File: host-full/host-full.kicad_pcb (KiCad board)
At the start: 4 copper layers, 117 x 129.5 mm, 201 parts, among them J1 CONN_INTEGRALSTICK_MCU_HOST, J10 PMOD_HOST, J11 PMOD_HOST, J12 PMOD_HOST, J13 PMOD_HOST, J14 PMOD_HOST, J15 XILINX_JTAG, J16 SMA, J17 SMA, J18 SMA, J19 SMA, J2 CONN_INTEGRALSTICK_FPGA_HOST, J20 SMA, J21 SMA, J22 TESTPAD, J23 PMOD_HOST, J24 TESTPAD, J25 TESTPAD, J26 TESTPAD, J27 TESTPAD, J28 TESTPAD, J29 TESTCLIP, J3 0826-1G1T-23-F, J30 TESTCLIP, J31 TESTCLIP, J4 0826-1G1T-23-F, J5 0826-1G1T-23-F, J6 0826-1G1T-23-F, J7 PMOD_HOST, J8 PMOD_HOST, J9 PMOD_HOST, K1 CONN_3_PWROUT, SW1 SW_SPST, SW2 SW_SPST, SW3 SW_SPST, U1 KSZ9031RNX, U2 KSZ9031RNX, U3 ECS-1612MV-250-CN-TR, U4 ECS-1612MV-250-CN-TR, U5 KSZ9031RNX, U6 ECS-1612MV-250-CN-TR, U7 SC185EUL

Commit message: Continued host-full layout. Almost all PHY RGMII routing done
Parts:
- added G***: LOGO, w_logo:Logo_silk_ROHS_5x2.8mm, F.Cu at (128.8, 89.8)
- added G***: LOGO, w_logo:Logo_silk_WEEE_3.4x5mm, F.Cu at (58.5, 41.8)
- added G***: LOGO, w_logo:Logo_silk_OSHW_6x6mm, F.Cu at (81.8, 40.8)
- added REF**: SERIALNUM_MOLEX_0916580020, azonenberg_pcb:SERIALNUM_MOLEX_0916580020, F.Cu at (34.5, 46.2)
- C10, C12, C14, C15, C16, C18, C19, C20, C22, C23, C24, C26, C28, C29, C30, C31, C32, C33, C34, C4, C59, C6, C60, C61, C62, C63, C64, C65, C66, C72, C73, C8, L4, R10, R20, R39, R40, R41, R42, R46, R47, R49, R50, R51: moved to B.Cu
- moved C40 57.0 mm to (50.8, 177.3)
- moved C42 57.0 mm to (48.1, 170.3)
- moved C45 57.0 mm to (32.2, 181.9)
- moved C50 57.0 mm to (32.4, 184.9)
- moved C51 57.0 mm to (40.5, 186.5)
- moved C52 57.0 mm to (38.0, 185.5)
- moved C54 57.0 mm to (31.5, 187.8)
- moved C69 57.0 mm to (39.2, 168.9)
- moved C83 57.0 mm to (41.8, 171.4)
- moved C84 57.0 mm to (46.2, 186.3)
- moved R32 57.0 mm to (29.8, 177.9)
- moved R36 57.0 mm to (32.6, 166.9)
- moved C39 57.0 mm to (35.2, 183.0)
- moved C47 57.0 mm to (45.5, 171.1)
- moved C48 57.0 mm to (44.9, 168.6)
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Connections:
- C10 pad 1: /1V8 -> /3V3
- C18 pad 1: /1V8 -> /3V3
- C2 pad 1: /1V8 -> /3V3
- C35 pad 1: /1V8 -> /3V3
- C38 pad 1: /3V3 -> /1V8
- C42 pad 1: /3V3 -> /1V8
- C46 pad 1: /3V3 -> /1V8
- C54 pad 1: /3V3 -> /1V8
- J1 pad 16: /Ethernet/ETH0_3_P -> /Ethernet/ETH0_3_N
- J1 pad 18: /Ethernet/ETH0_3_N -> /Ethernet/ETH0_3_P
- J1 pad 4: /Ethernet/ETH0_1_P -> /Ethernet/ETH0_1_N
- J1 pad 6: /Ethernet/ETH0_1_N -> /Ethernet/ETH0_1_P
- J18 pad 1: /LVDS_DQ0_P -> /LVDS_DQ1_N
- J19 pad 1: /LVDS_DQ0_N -> /LVDS_DQ1_P
- J2 pad 10: (no net) -> /LVDS_DQ8_N
- J2 pad 101: /Ethernet/ETH3_TXD2 -> /Ethernet/ETH1_TX_CLK
- J2 pad 102: /Ethernet/ETH3_TXD3 -> /Ethernet/ETH2_RXD3
- J2 pad 103: /Ethernet/ETH3_TX_CLK -> /Ethernet/ETH1_TXD3
- J2 pad 104: /Ethernet/ETH3_TX_EN -> /Ethernet/ETH2_TX_EN
- J2 pad 108: /Ethernet/ETH3_RXD3 -> /Ethernet/ETH2_TX_CLK
- J2 pad 110: /Ethernet/ETH3_RXD2 -> /Ethernet/ETH2_TXD3
- J2 pad 113: /Ethernet/ETH3_RXD1 -> /Ethernet/ETH1_TXD2
- J2 pad 114: /Ethernet/ETH3_RXD0 -> /Ethernet/ETH2_TXD2
- J2 pad 115: /Ethernet/ETH3_RX_DV -> /Ethernet/ETH1_TXD1
- J2 pad 116: /Ethernet/ETH3_MDC -> /Ethernet/ETH2_TXD1
- J2 pad 119: /Ethernet/ETH3_MDIO -> /Ethernet/ETH1_TXD0
- J2 pad 12: (no net) -> /LVDS_DQ8_P
- J2 pad 120: /Ethernet/ETH3_RST_N -> /Ethernet/ETH2_TXD0
- J2 pad 16: (no net) -> /LVDS_DQ6_N
- J2 pad 18: (no net) -> /LVDS_DQ6_P
- J2 pad 21: /LVDS_DQ5_N -> (no net)
- J2 pad 23: /LVDS_DQ5_P -> (no net)
- J2 pad 27: /LVDS_DQ3_N -> (no net)
- J2 pad 29: /LVDS_DQ3_P -> (no net)
- J2 pad 41: /Ethernet/ETH1_RX_CLK -> /Ethernet/ETH3_RX_CLK
- J2 pad 42: /Ethernet/ETH1_TXD0 -> /Ethernet/ETH3_MDIO
- J2 pad 43: /Ethernet/ETH1_LED1_N_1V8 -> /Ethernet/ETH3_MDC
- J2 pad 44: /Ethernet/ETH1_TXD1 -> /Ethernet/ETH3_RST_N
- J2 pad 47: /Ethernet/ETH1_TXD2 -> /Ethernet/ETH3_RX_DV
- J2 pad 48: /Ethernet/ETH1_TXD3 -> (no net)
- J2 pad 49: /Ethernet/ETH1_TX_CLK -> /Ethernet/ETH3_RXD0
- J2 pad 50: /Ethernet/ETH1_TX_EN -> /Ethernet/ETH3_LED2_N_1V8
- J2 pad 53: /Ethernet/ETH1_RST_N -> /Ethernet/ETH3_RXD1
- J2 pad 54: (no net) -> /Ethernet/ETH3_LED1_N_1V8
- J2 pad 55: (no net) -> /Ethernet/ETH3_RXD2
- J2 pad 56: /Ethernet/ETH1_MDC -> (no net)
- J2 pad 59: /Ethernet/ETH1_MDIO -> /Ethernet/ETH3_RXD3
- J2 pad 60: /Ethernet/ETH1_RXD3 -> (no net)
- J2 pad 61: /Ethernet/ETH1_RXD2 -> /Ethernet/ETH3_TXD2
- J2 pad 62: /Ethernet/ETH1_RXD1 -> /Ethernet/ETH3_TX_EN
- J2 pad 65: /Ethernet/ETH1_RXD0 -> /Ethernet/ETH3_TXD1
- J2 pad 66: /Ethernet/ETH1_RX_DV -> /Ethernet/ETH3_TX_CLK
- J2 pad 67: /Ethernet/ETH1_LED2_N_1V8 -> /Ethernet/ETH3_TXD0
- J2 pad 68: (no net) -> /Ethernet/ETH3_TXD3
- J2 pad 71: /Ethernet/ETH2_RX_CLK -> /Ethernet/ETH1_RX_CLK
- J2 pad 72: /Ethernet/ETH3_RX_CLK -> /Ethernet/ETH2_RX_CLK
- J2 pad 73: /Ethernet/ETH2_TXD0 -> /Ethernet/ETH1_RST_N
- J2 pad 74: /Ethernet/ETH2_TXD1 -> /Ethernet/ETH3_LED2_N
- J2 pad 77: /Ethernet/ETH2_TXD2 -> /Ethernet/ETH1_MDIO
- J2 pad 78: /Ethernet/ETH2_TXD3 -> /Ethernet/ETH3_LED1_N
- J2 pad 79: /Ethernet/ETH2_TX_CLK -> /Ethernet/ETH1_MDC
- J2 pad 80: /Ethernet/ETH2_TX_EN -> /Ethernet/ETH2_RST_N
- J2 pad 83: /Ethernet/ETH2_RXD3 -> /Ethernet/ETH1_RX_DV
- J2 pad 84: /Ethernet/ETH2_RXD2 -> /Ethernet/ETH2_MDIO
- J2 pad 85: /Ethernet/ETH2_RXD1 -> /Ethernet/ETH1_RXD0
- J2 pad 86: /Ethernet/ETH2_RXD0 -> /Ethernet/ETH2_MDC
- J2 pad 89: /Ethernet/ETH2_RX_DV -> /Ethernet/ETH1_RXD1
- J2 pad 90: /Ethernet/ETH2_MDC -> /Ethernet/ETH2_RX_DV
- J2 pad 91: /Ethernet/ETH2_MDIO -> /Ethernet/ETH1_RXD2
- J2 pad 92: /Ethernet/ETH2_RST_N -> /Ethernet/ETH2_RXD0
- J2 pad 95: /Ethernet/ETH1_LED1_N -> /Ethernet/ETH1_RXD3
- J2 pad 96: /Ethernet/ETH1_LED2_N -> /Ethernet/ETH2_RXD1
- J2 pad 97: /Ethernet/ETH3_TXD0 -> /Ethernet/ETH1_TX_EN
- J2 pad 98: /Ethernet/ETH3_TXD1 -> /Ethernet/ETH2_RXD2
- J20 pad 1: /LVDS_DQ1_P -> /LVDS_DQ0_N
- J21 pad 1: /LVDS_DQ1_N -> /LVDS_DQ0_P
- J23 pad 1: /LVDS_DQ2_P -> /LVDS_DQ8_N
- J23 pad 10: /LVDS_DQ5_N -> /LVDS_DQ2_P
- J23 pad 2: /LVDS_DQ2_N -> /LVDS_DQ8_P
- J23 pad 3: /LVDS_DQ3_P -> /LVDS_DQ4_N
- J23 pad 4: /LVDS_DQ3_N -> /LVDS_DQ4_P
- J23 pad 7: /LVDS_DQ4_P -> /LVDS_DQ6_N
- J23 pad 8: /LVDS_DQ4_N -> /LVDS_DQ6_P
- J23 pad 9: /LVDS_DQ5_P -> /LVDS_DQ2_N
- R1 pad 2: /Ethernet/ETH1_LED2_N_1V8 -> /Ethernet/ETH1_LED2_N
- R17 pad 1: /1V8 -> /3V3
- R19 pad 2: /Ethernet/ETH1_LED1_N_1V8 -> /Ethernet/ETH1_LED1_N
- R23 pad 1: /1V8 -> /3V3
- R25 pad 2: /Ethernet/ETH3_LED2_N -> /Ethernet/ETH3_LED2_N_1V8
- R34 pad 2: /Ethernet/ETH3_LED1_N -> /Ethernet/ETH3_LED1_N_1V8
- R36 pad 1: /3V3 -> /1V8
- R8 pad 1: /1V8 -> /3V3
- U1 pad 10: /Ethernet/ETH1_4_P -> /Ethernet/ETH1_4_N
- U1 pad 11: /Ethernet/ETH1_4_N -> /Ethernet/ETH1_4_P
- U1 pad 15: /Ethernet/ETH1_LED2_N_1V8 -> /Ethernet/ETH1_LED2_N
- U1 pad 16: /1V8 -> /3V3
- U1 pad 17: /Ethernet/ETH1_LED1_N_1V8 -> /Ethernet/ETH1_LED1_N
- U1 pad 34: /1V8 -> /3V3
- U1 pad 40: /1V8 -> /3V3
- U1 pad 5: /Ethernet/ETH1_2_P -> /Ethernet/ETH1_2_N
- U1 pad 6: /Ethernet/ETH1_2_N -> /Ethernet/ETH1_2_P
- U2 pad 10: /Ethernet/ETH2_4_P -> /Ethernet/ETH2_4_N
- U2 pad 11: /Ethernet/ETH2_4_N -> /Ethernet/ETH2_4_P
- U2 pad 5: /Ethernet/ETH2_2_P -> /Ethernet/ETH2_2_N
- U2 pad 6: /Ethernet/ETH2_2_N -> /Ethernet/ETH2_2_P
- U3 pad 1: /1V8 -> /3V3
- U3 pad 4: /1V8 -> /3V3
- U5 pad 10: /Ethernet/ETH3_4_P -> /Ethernet/ETH3_4_N
- U5 pad 11: /Ethernet/ETH3_4_N -> /Ethernet/ETH3_4_P
- U5 pad 15: /Ethernet/ETH3_LED2_N -> /Ethernet/ETH3_LED2_N_1V8
- U5 pad 16: /3V3 -> /1V8
- U5 pad 17: /Ethernet/ETH3_LED1_N -> /Ethernet/ETH3_LED1_N_1V8
- U5 pad 34: /3V3 -> /1V8
- U5 pad 40: /3V3 -> /1V8
- U5 pad 5: /Ethernet/ETH3_2_P -> /Ethernet/ETH3_2_N
- U5 pad 6: /Ethernet/ETH3_2_N -> /Ethernet/ETH3_2_P
- U6 pad 1: /3V3 -> /1V8
- U6 pad 4: /3V3 -> /1V8
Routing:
- net /GND: track 380.4 -> 1004.3 mm, vias 26 -> 148
- net /3V3: track 334.4 -> 722.3 mm, vias 35 -> 78
- net /1V2: track 0.00 -> 147.2 mm, vias 0 -> 19
- net /2V5: track 0.00 -> 141.3 mm, vias 0 -> 17
- net /Ethernet/ETH1_TXD0: track 0.00 -> 109.4 mm
- net /Ethernet/ETH1_TXD1: track 0.00 -> 107.1 mm
- net /Ethernet/ETH2_TXD0: track 0.00 -> 106.0 mm, vias 0 -> 2
- net /Ethernet/ETH1_TXD2: track 0.00 -> 105.4 mm
- net /Ethernet/ETH2_TXD1: track 0.00 -> 103.6 mm, vias 0 -> 2
- net /Ethernet/ETH1_TXD3: track 0.00 -> 102.8 mm
- net /Ethernet/ETH2_TXD2: track 0.00 -> 102.0 mm, vias 0 -> 2
- net /Ethernet/ETH1_TX_CLK: track 0.00 -> 100.2 mm
- net /Ethernet/ETH2_TXD3: track 0.00 -> 98.3 mm, vias 0 -> 2
- net /Ethernet/ETH1_TX_EN: track 0.00 -> 97.2 mm
- net /Ethernet/ETH2_TX_CLK: track 0.00 -> 96.5 mm, vias 0 -> 2
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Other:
- board text added: "INTEGRALSTICK Quad Ethernet Host A. Zonenberg / v0.1 / 2019-11-09"

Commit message: Finished initial routing, still need to do planes and design review
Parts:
- C37, C39, C40, C41, C42, C43, C44, C46, C47, C48, C50, C51, C52, C53, C67, C68, C69, C70, C74, C75, C82, L10, L5, L6, R43, R44, R48, R54: moved to B.Cu
- L11: footprint azonenberg_pcb:EIA_0402_RES_NOSILK -> azonenberg_pcb:INDUCTOR_YUDEN_NRS5030
- moved J26 72.3 mm to (99.8, 114.0)
- moved J27 68.7 mm to (99.8, 111.2)
- moved J24 65.4 mm to (82.3, 116.2)
- moved C51 63.6 mm to (46.8, 123.2), turned to 270 degrees
- moved C50 63.4 mm to (49.5, 123.8), turned to 180 degrees
- moved C52 63.0 mm to (47.6, 123.2), turned to 270 degrees
- moved C38 62.5 mm to (40.2, 122.8), turned to 90 degrees
- moved C54 58.9 mm to (38.2, 129.3)
- moved C84 55.7 mm to (44.8, 130.7), turned to 270 degrees
- moved C39 54.7 mm to (41.4, 128.7)
- moved C43 54.4 mm to (41.5, 125.7), turned to 180 degrees
- moved R32 54.3 mm to (40.8, 124.8)
- moved R33 54.0 mm to (40.6, 128.2)
- moved C45 53.9 mm to (48.8, 130.7), turned to 270 degrees
- moved C44 53.0 mm to (49.0, 127.7), turned to 180 degrees
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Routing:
- net /GND: track 1004.3 -> 1161.9 mm, vias 148 -> 197
- net /1V2: track 147.2 -> 261.7 mm, vias 19 -> 40
- net /ETH0_LED1_P: track 0.00 -> 111.2 mm, vias 0 -> 1
- net /ETH0_LED2_P: track 0.00 -> 102.2 mm, vias 0 -> 1
- net /Ethernet/ETH3_LED1_N: track 0.00 -> 89.4 mm, vias 0 -> 2
- net /1V8: track 35.3 -> 114.1 mm, vias 10 -> 21
- net /Ethernet/ETH3_LED2_N: track 0.00 -> 77.7 mm, vias 0 -> 1
- net /Ethernet/ETH3_LED2_N_1V8: track 1.85 -> 74.7 mm, vias 0 -> 2
- net /Ethernet/ETH3_LED1_N_1V8: track 1.85 -> 73.3 mm, vias 0 -> 2
- net /Ethernet/ETH3_RST_N: track 0.00 -> 59.2 mm, vias 0 -> 2
- net /Power Supply/5V0: track 60.0 -> 115.3 mm, vias 7 -> 25
- net /Ethernet/ETH3_MDIO: track 0.00 -> 55.1 mm, vias 0 -> 2
- net /2V5: track 141.3 -> 183.6 mm, vias 17 -> 20
- net /3V3: track 722.3 -> 758.7 mm, vias 78 -> 81
- net /Ethernet/ETH3_A2V5: track 0.00 -> 15.2 mm, vias 0 -> 5
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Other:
- board text added: "1V2"
- board text added: "2V5"
- board text added: "3V3"
- board text added: "5V0"
- board text added: "5VDC"
- board text added: "CLK_N"
- board text added: "CLK_P"
- board text added: "D0_N"
- board text added: "D0_P"
- board text added: "D1_N"
- board text added: "D1_P"
- board text added: "E0>"
- board text added: "E1>"
- board text added: "E2>"
- board text added: "E3>"
- board text added: "FPGA LVDS"
- board text added: "GND"
- board text added: "INTEGRALSTICK Quad Ethernet Host A. Zonenberg / v0.1 / 2019-11-10"
- board text added: "JTAG"
- board text removed: "INTEGRALSTICK Quad Ethernet Host A. Zonenberg / v0.1 / 2019-11-09"

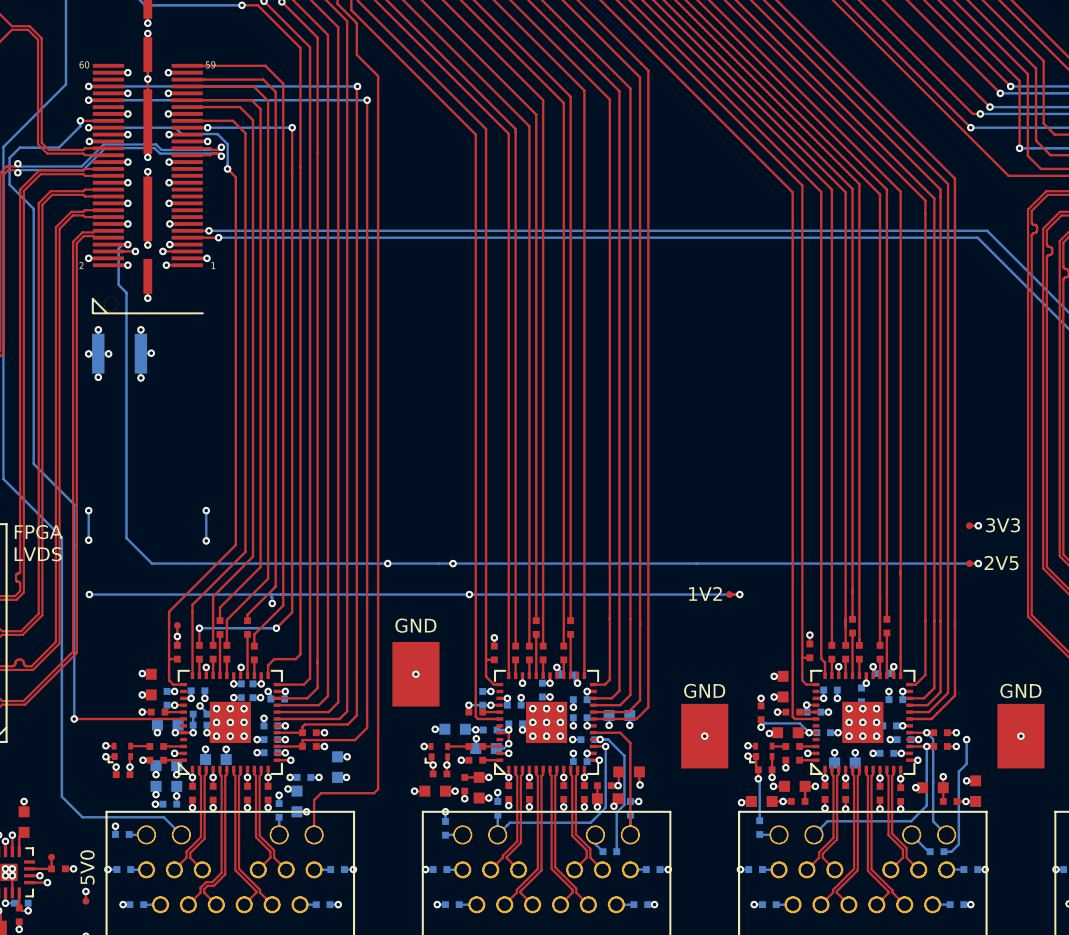
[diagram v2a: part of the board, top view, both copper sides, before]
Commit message: Initial plane layout. Still need more work on power layers.
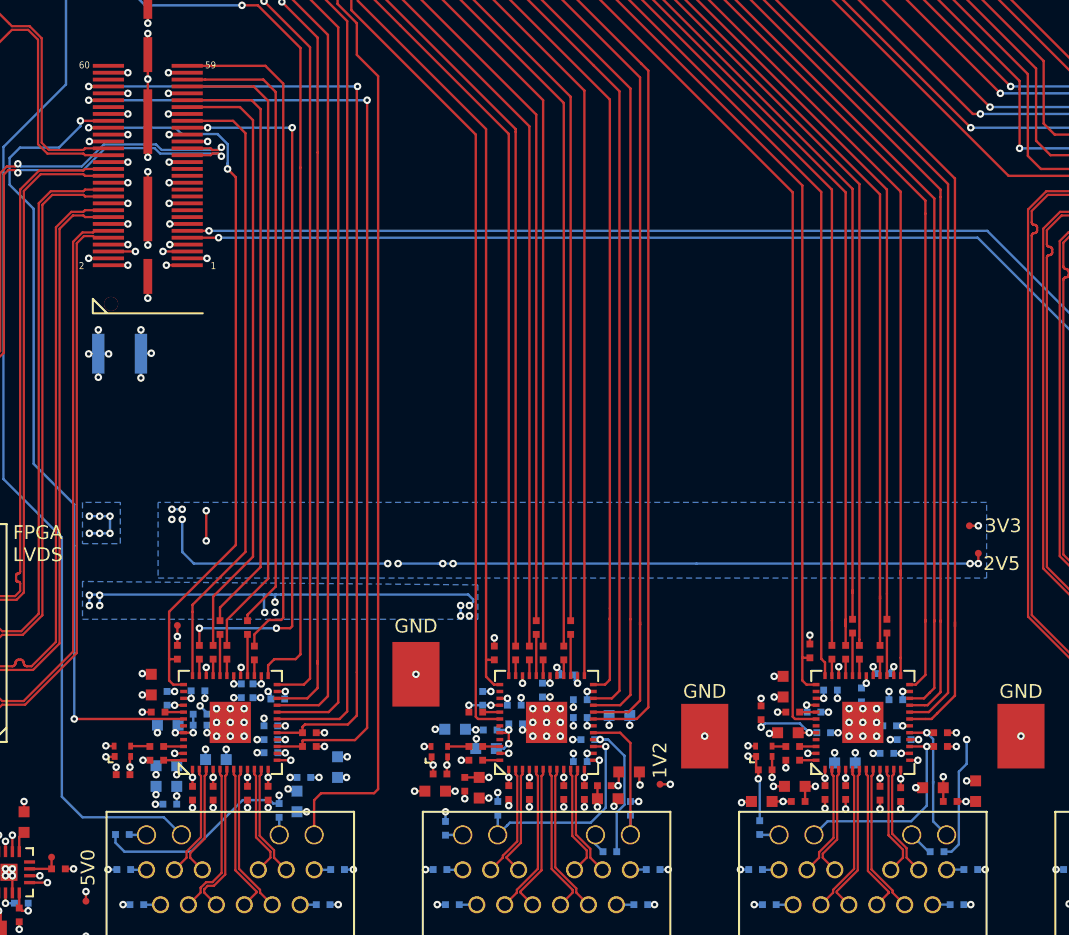
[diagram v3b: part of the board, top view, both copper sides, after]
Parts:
- moved J24 14.7 mm to (77.2, 130.0)
- moved J26 0.99 mm to (100.4, 113.2)
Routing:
- net /1V2: track 261.7 -> 243.1 mm, vias 40 -> 48
- net /3V3: track 758.7 -> 749.9 mm, vias 81 -> 80
- net /Power Supply/5V0: track 115.3 -> 121.4 mm, vias 25 -> 29
- net /2V5: track 183.6 -> 189.5 mm, vias 20 -> 27
- net /1V8: track 114.1 -> 116.0 mm
- net /Ethernet/ETH1_A1V2: track 9.25 -> 10.6 mm
- net /Ethernet/ETH3_RX_CLK: track 51.4 -> 51.9 mm
- net /Ethernet/ETH3_RXD3: track 49.3 -> 49.8 mm
- added copper zone on B.Cu, net /1V2
- added copper zone on In2.Cu, net /1V2
- added copper zone on B.Cu, net /2V5
- added copper zone on In2.Cu, net /2V5
- added copper zone on In2.Cu, net /3V3
- added copper zone on In2.Cu, net /Ethernet/ETH1_A1V2
- added copper zone on In2.Cu, net /Ethernet/ETH1_A2V5
- added copper zone on In2.Cu, net /Ethernet/ETH2_A1V2
- added copper zone on In2.Cu, net /Ethernet/ETH2_A2V5
- added copper zone on In1.Cu, net /GND
- added copper zone on B.Cu, net /Power Supply/5V0
- added copper zone on In2.Cu, net /Power Supply/5V0

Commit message: Finished tweaking zone fills. Ready for signoff review.
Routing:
- net /1V2: track 243.1 -> 250.9 mm
- net /Ethernet/ETH3_A1V2: track 9.51 -> 13.9 mm
- net /1V8: track 116.0 -> 117.8 mm
- added copper zone on In2.Cu, net /1V8
- added copper zone on In2.Cu, net /Ethernet/ETH3_A1V2
- added copper zone on In2.Cu, net /Ethernet/ETH3_A2V5

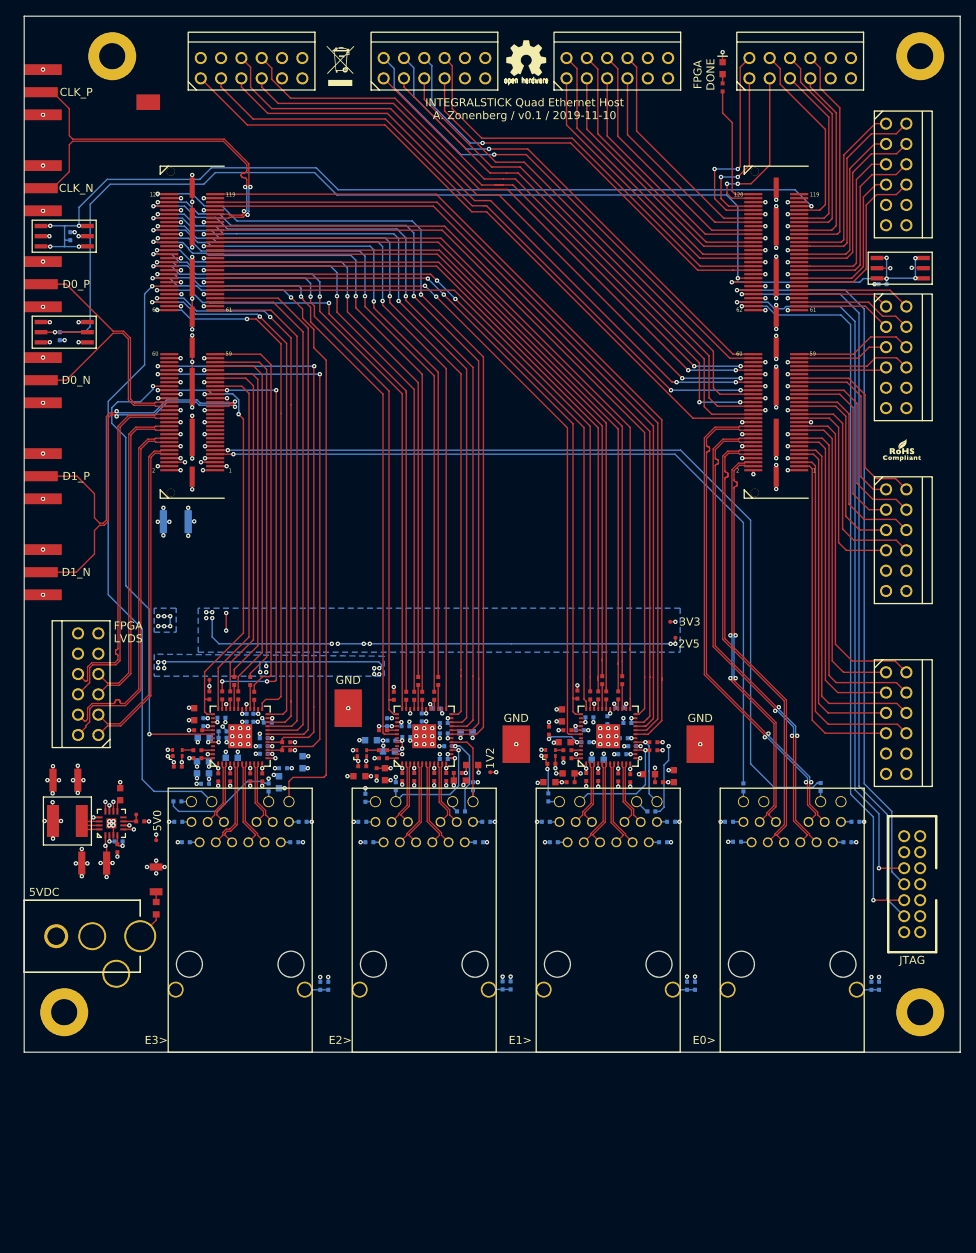
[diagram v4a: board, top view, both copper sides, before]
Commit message: Various fixes during layout review, added some silkscreen labels and a layer-change cap
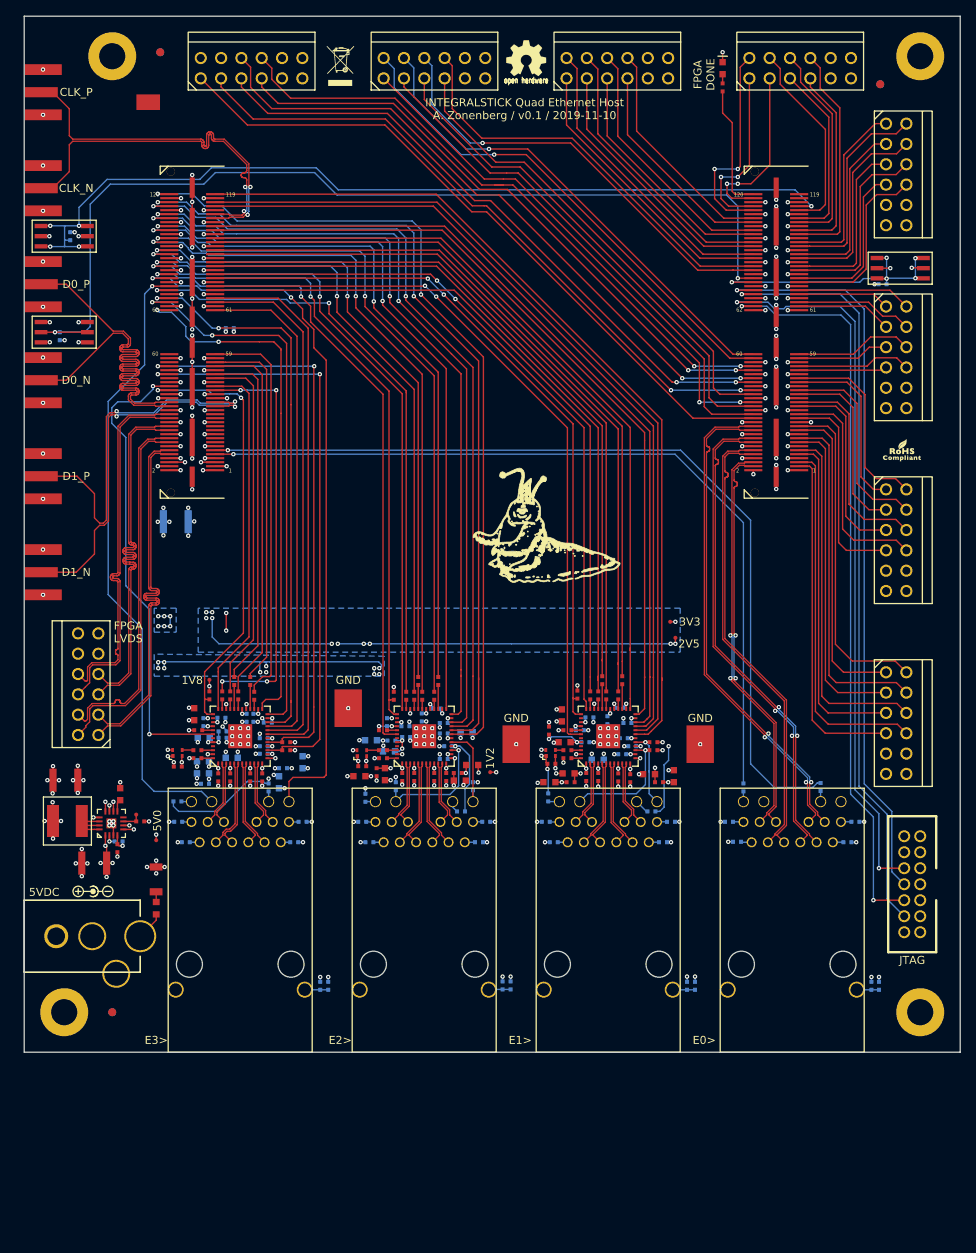
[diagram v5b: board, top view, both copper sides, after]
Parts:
- added C89: 0.47 uF, azonenberg_pcb:EIA_0402_CAP_NOSILK, B.Cu at (44.7, 74.5)
- added FIDUCIAL_1MM: VAL**, azonenberg_pcb:FIDUCIAL_1MM, B.Cu at (30.0, 160.0)
- added FIDUCIAL_1MM: VAL**, azonenberg_pcb:FIDUCIAL_1MM, B.Cu at (126.0, 44.0)
- added FIDUCIAL_1MM: VAL**, azonenberg_pcb:FIDUCIAL_1MM, B.Cu at (36.0, 40.0)
- added FIDUCIAL_1MM: VAL**, azonenberg_pcb:FIDUCIAL_1MM, F.Cu at (30.0, 160.0)
- added FIDUCIAL_1MM: VAL**, azonenberg_pcb:FIDUCIAL_1MM, F.Cu at (126.0, 44.0)
- added FIDUCIAL_1MM: VAL**, azonenberg_pcb:FIDUCIAL_1MM, F.Cu at (36.0, 40.0)
- added G***: LOGO, azonenberg_pcb:LONGTHING-600DPI, F.Cu at (85.4, 99.9)
- added G***: LOGO, w_logo:Logo_silk_polarity_center_5x1.4mm, F.Cu at (27.6, 144.9)
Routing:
- net /LVDS_DQ0_N: track 26.7 -> 45.4 mm
- net /LVDS_DQ0_P: track 26.7 -> 45.4 mm
- net /GND: track 1161.9 -> 1168.3 mm, vias 197 -> 198
- net /LVDS_DQ4_P: track 40.1 -> 45.5 mm
- net /LVDS_DQ4_N: track 40.1 -> 45.5 mm
- net /1V8: track 117.8 -> 122.5 mm, vias 21 -> 22
- net /LVDS_DQ8_N: track 41.0 -> 45.4 mm
- net /LVDS_DQ8_P: track 41.0 -> 45.4 mm
- net /LVDS_CLK_P: track 42.5 -> 45.4 mm
- net /LVDS_CLK_N: track 42.5 -> 45.4 mm
- net /LVDS_DQ2_P: track 44.0 -> 45.4 mm
- net /LVDS_DQ2_N: track 44.0 -> 45.4 mm
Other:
- board text added: "1V8"
- board text added: "Place UL mark and date code in this area"
